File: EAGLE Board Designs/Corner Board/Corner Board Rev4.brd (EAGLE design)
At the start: 64.8 x 44.5 mm, 61 parts, among them J1 CONNECTOR-8_AMPHENOL_M12A_08P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, J2 CONNECTOR-2_MICROFIT_SMD_RIGH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, J3 BINDER-M12-A_4_PIN, J4 CONNECTOR-4_μF_S_RA_, T1 78613/3C_78613/3C_AIRGAP, U1 OPAMP_2_CHANNEL_OPA_2991, U10 LTC6820, U11 MCP3204, U3 INA823DT, U4 OPAMP_2_CHANNEL_OPA_2991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

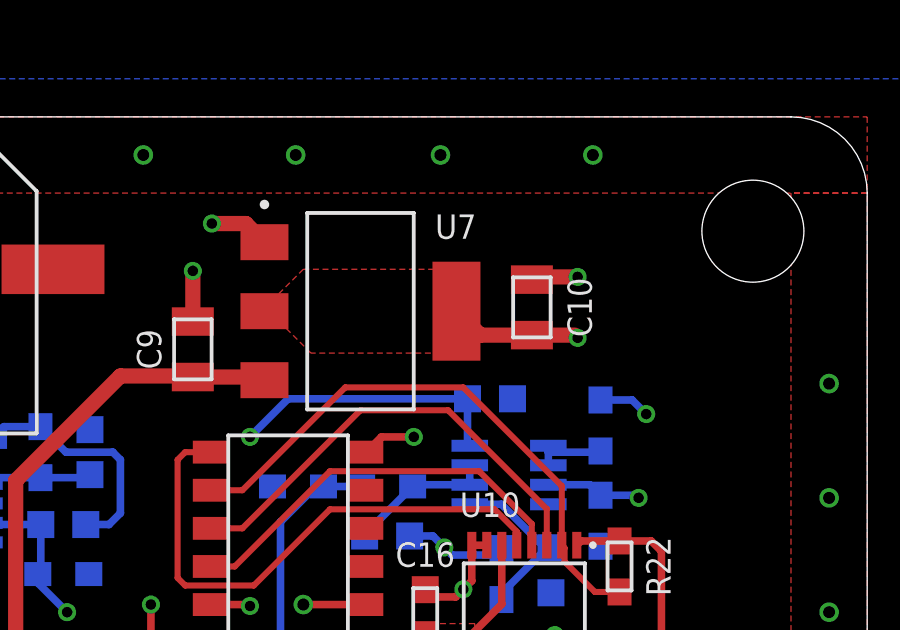
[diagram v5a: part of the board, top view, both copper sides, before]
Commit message: more power vias
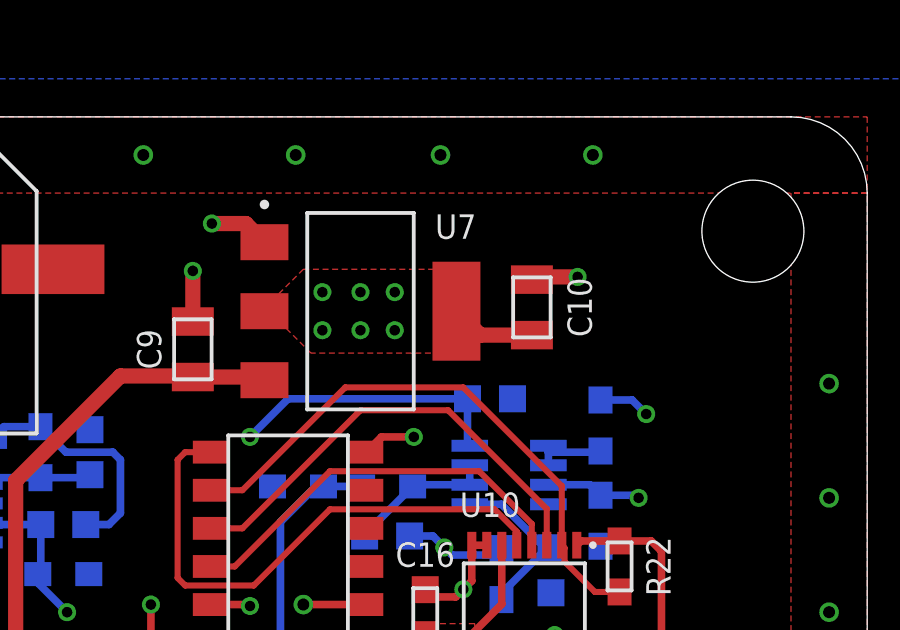
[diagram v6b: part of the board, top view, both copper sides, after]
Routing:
- net +3V3: track 68.8 -> 80.0 mm, vias 5 -> 10
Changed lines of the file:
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@@
 <grid distance="10" unitdist="mil" unit="mil" style="lines" multiple="1" display="yes" altdistance="5" altunitdist="mil" altunit="mil"/>
 <layers>
-<layer number="1" name="Top" color="4" fill="1" visible="no" active="yes"/>
-<layer number="2" name="Route2" color="16" fill="1" visible="no" active="yes"/>
+<layer number="1" name="Top" color="4" fill="1" visible="yes" active="yes"/>
+<layer number="2" name="Route2" color="16" fill="1" visible="yes" active="yes"/>
 <layer number="3" name="Route3" color="17" fill="1" visible="no" active="no"/>
 <layer number="4" name="Route4" color="18" fill="1" visible="no" active="no"/>
@@
 <layer number="17" name="Pads" color="2" fill="1" visible="yes" active="yes"/>
 <layer number="18" name="Vias" color="2" fill="1" visible="yes" active="yes"/>
-<layer number="19" name="Unrouted" color="6" fill="1" visible="no" active="yes"/>
+<layer number="19" name="Unrouted" color="6" fill="1" visible="yes" active="yes"/>
 <layer number="20" name="Dimension" color="24" fill="1" visible="yes" active="yes"/>
-<layer number="21" name="tPlace" color="7" fill="1" visible="no" active="yes"/>
+<layer number="21" name="tPlace" color="7" fill="1" visible="yes" active="yes"/>
 <layer number="22" name="bPlace" color="7" fill="1" visible="yes" active="yes"/>
-<layer number="23" name="tOrigins" color="15" fill="1" visible="no" active="yes"/>
+<layer number="23" name="tOrigins" color="15" fill="1" visible="yes" active="yes"/>
 <layer number="24" name="bOrigins" color="15" fill="1" visible="yes" active="yes"/>
-<layer number="25" name="tNames" color="7" fill="1" visible="no" active="yes"/>
+<layer number="25" name="tNames" color="7" fill="1" visible="yes" active="yes"/>
 <layer number="26" name="bNames" color="7" fill="1" visible="yes" active="yes"/>
 <layer number="27" name="tValues" color="7" fill="1" visible="no" active="yes"/>
@@
 <layer number="37" name="tTest" color="7" fill="1" visible="no" active="yes"/>
 <layer number="38" name="bTest" color="7" fill="1" visible="no" active="yes"/>
-<layer number="39" name="tKeepout" color="4" fill="11" visible="no" active="yes"/>
+<layer number="39" name="tKeepout" color="4" fill="11" visible="yes" active="yes"/>
 <layer number="40" name="bKeepout" color="1" fill="11" visible="yes" active="yes"/>
-<layer number="41" name="tRestrict" color="4" fill="10" visible="no" active="yes"/>
+<layer number="41" name="tRestrict" color="4" fill="10" visible="yes" active="yes"/>
 <layer number="42" name="bRestrict" color="1" fill="10" visible="yes" active="yes"/>
 <layer number="43" name="vRestrict" color="2" fill="10" visible="no" active="yes"/>
@@
 <layer number="49" name="Reference" color="7" fill="1" visible="no" active="yes"/>
 <layer number="50" name="dxf" color="7" fill="1" visible="no" active="no"/>
-<layer number="51" name="tDocu" color="7" fill="1" visible="no" active="yes"/>
+<layer number="51" name="tDocu" color="7" fill="1" visible="yes" active="yes"/>
 <layer number="52" name="bDocu" color="7" fill="1" visible="yes" active="yes"/>
 <layer number="53" name="tGND_GNDA" color="7" fill="9" visible="no" active="no"/>
@@
 <wire x1="60.452" y1="29.21" x2="57.912" y2="26.67" width="0.508" layer="15"/>
 <wire x1="57.912" y1="29.972" x2="57.912" y2="26.67" width="0.254" layer="1"/>
-<wire x1="53.594" y1="37.175" x2="55.027" y2="37.175" width="0.508" layer="1"/>
-<wire x1="55.027" y1="37.175" x2="55.118" y2="37.084" width="0.254" layer="1"/>
-<via x="55.118" y="37.084" extent="1-16" drill="0.35"/>
-<wire x1="55.118" y1="37.084" x2="58.674" y2="37.084" width="0.508" layer="15"/>
-<wire x1="58.674" y1="37.084" x2="60.452" y2="35.306" width="0.508" layer="15"/>
+<wire x1="60.452" y1="35.306" x2="57.785" y2="37.973" width="0.508" layer="15"/>
 <wire x1="52.59" y1="30.1725" x2="52.59" y2="28.206" width="0.254" layer="1"/>
 <wire x1="52.59" y1="28.206" x2="51.59" y2="27.206" width="0.254" layer="1"/>
@@
 <wire x1="34.786" y1="28.206" x2="34.786" y2="28.575" width="0.254" layer="16"/>
 <wire x1="37.338" y1="25.654" x2="34.786" y2="28.206" width="0.254" layer="16"/>
+<via x="46.609" y="38.608" extent="1-16" drill="0.35"/>
+<via x="47.879" y="38.608" extent="1-16" drill="0.35"/>
+<via x="49.022" y="38.608" extent="1-16" drill="0.35"/>
+<via x="46.609" y="37.338" extent="1-16" drill="0.35"/>
+<via x="47.879" y="37.338" extent="1-16" drill="0.35"/>
+<via x="49.022" y="37.338" extent="1-16" drill="0.35"/>
+<wire x1="57.785" y1="37.973" x2="49.022" y2="37.973" width="0.508" layer="15"/>
+<wire x1="49.022" y1="37.973" x2="49.022" y2="37.338" width="0.508" layer="15"/>
+<wire x1="49.022" y1="38.608" x2="49.022" y2="37.973" width="0.508" layer="15"/>
+<wire x1="46.609" y1="37.973" x2="46.609" y2="38.608" width="0.508" layer="15"/>
+<wire x1="49.022" y1="37.973" x2="47.879" y2="37.973" width="0.508" layer="15"/>
+<wire x1="47.879" y1="37.973" x2="46.609" y2="37.973" width="0.508" layer="15"/>
+<wire x1="46.609" y1="37.338" x2="46.609" y2="37.973" width="0.508" layer="15"/>
+<wire x1="47.879" y1="37.338" x2="47.879" y2="37.973" width="0.508" layer="15"/>
+<wire x1="47.879" y1="38.608" x2="47.879" y2="37.973" width="0.508" layer="15"/>
 </signal>
 <signal name="OUT_P">
